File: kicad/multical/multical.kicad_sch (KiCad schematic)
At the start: 55 parts, among them J10 Screw_Terminal_01x02, J11 Screw_Terminal_01x02, J12 Screw_Terminal_01x02, J13 Screw_Terminal_01x02, J14 Screw_Terminal_01x02, J15 Screw_Terminal_01x02, J16 Screw_Terminal_01x02, J17 Screw_Terminal_01x02, J18 Screw_Terminal_01x02, K1 Relay_SPDT, K2 Relay_SPDT, K3 Relay_SPDT, K4 Relay_SPDT, K5 Relay_SPDT, K6 Relay_SPDT, K7 Relay_SPDT, K8 Relay_SPDT, U1 ESP32-WROOM-32, U10 HLK-PM01, U11 AMS1117-3.3, U12 zmpt101b, U13 ULN2003A, U14 ULN2003A, U2 ACS712xLCTR-20A, U3 ACS712xLCTR-20A, U4 ACS712xLCTR-20A, U5 ACS712xLCTR-20A, U6 ACS712xLCTR-20A, U7 ACS712xLCTR-20A, U8 ACS712xLCTR-20A, U9 ACS712xLCTR-20A

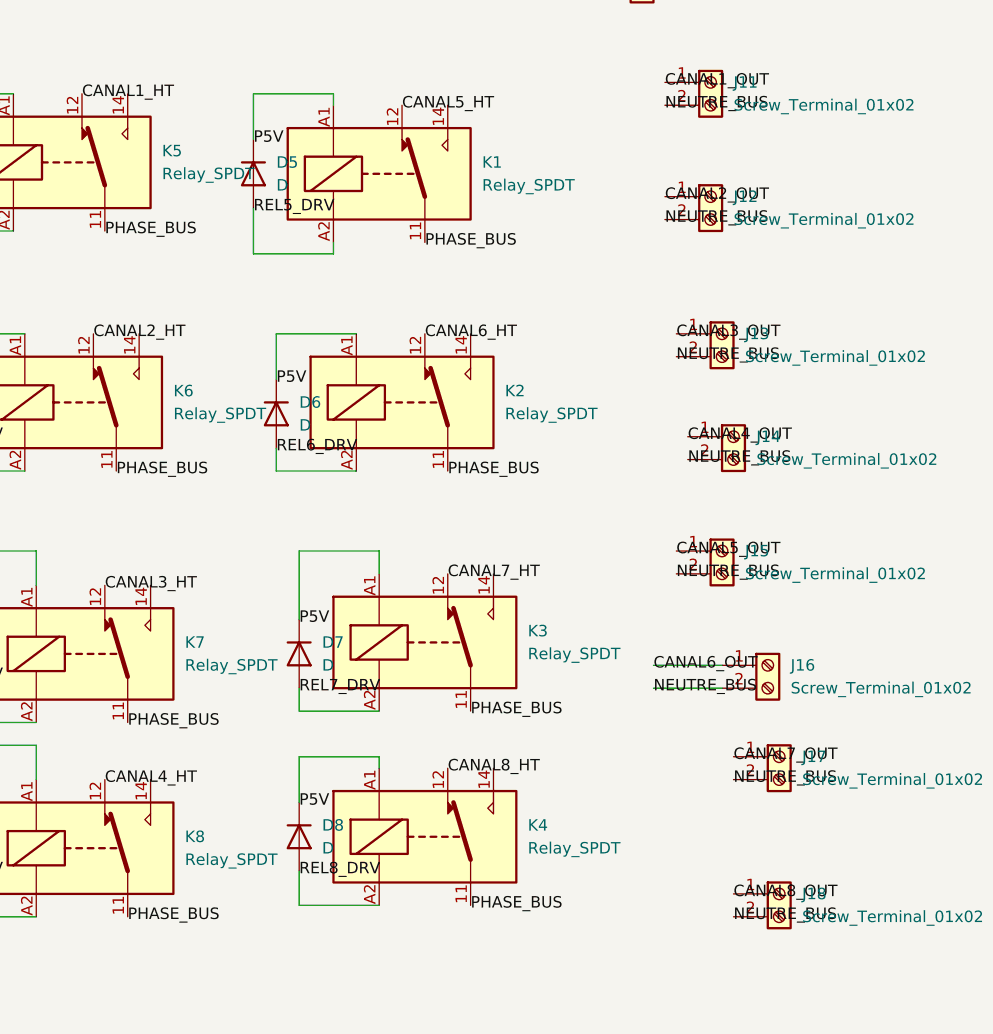
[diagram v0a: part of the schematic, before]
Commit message: Routage PCB 20A, schema de branchement et mise a jour de la presentation
- kicad/ : outils et guide de routage pour tenir 20A (GUIDE_ROUTAGE_20A,
  fix_dsn_widths_20A.py, replan_pcb_20A.py, strip_tracks.py), PCB/schema
  mis a jour en consequence. Routage non termine : il reste 10 pistes a
  tracer (cf. README racine).
- schema_branchement.png et diagramme_cas_utilisation.drawio ajoutes
- presentation de soutenance et GUIDE_MAQUETTE_BOITIER mis a jour
- retire l'ancienne sauvegarde du rapport (avant corrections)

Co-Authored-By: Claude Sonnet 5 <noreply@anthropic.com>
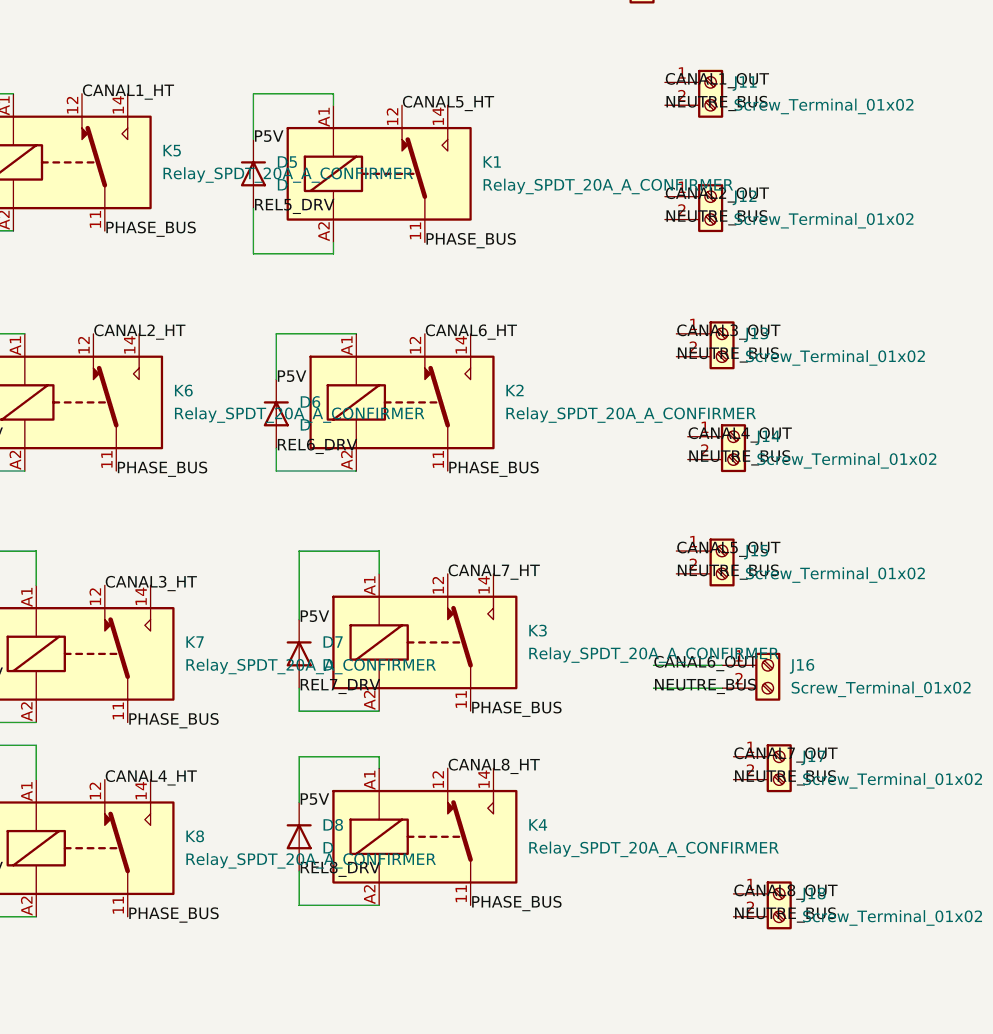
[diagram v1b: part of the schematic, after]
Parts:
- K1, K2, K3, K4, K5, K6, K7, K8: value Relay_SPDT -> Relay_SPDT_20A_A_CONFIRMER
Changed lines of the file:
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@@
 			)
 		)
-		(property "Value" "Relay_SPDT"
+		(property "Value" "Relay_SPDT_20A_A_CONFIRMER"
 			(at 210.82 119.3799 0)
 			(show_name no)
@@
 			)
 		)
-		(property "Value" "Relay_SPDT"
+		(property "Value" "Relay_SPDT_20A_A_CONFIRMER"
 			(at 243.84 44.4499 0)
 			(show_name no)
@@
 			)
 		)
-		(property "Value" "Relay_SPDT"
+		(property "Value" "Relay_SPDT_20A_A_CONFIRMER"
 			(at 246.38 69.8499 0)
 			(show_name no)
@@
 			)
 		)
-		(property "Value" "Relay_SPDT"
+		(property "Value" "Relay_SPDT_20A_A_CONFIRMER"
 			(at 209.55 69.8499 0)
 			(show_name no)
@@
 			)
 		)
-		(property "Value" "Relay_SPDT"
+		(property "Value" "Relay_SPDT_20A_A_CONFIRMER"
 			(at 248.92 118.1099 0)
 			(show_name no)
@@
 			)
 		)
-		(property "Value" "Relay_SPDT"
+		(property "Value" "Relay_SPDT_20A_A_CONFIRMER"
 			(at 248.92 96.5199 0)
 			(show_name no)
@@
 			)
 		)
-		(property "Value" "Relay_SPDT"
+		(property "Value" "Relay_SPDT_20A_A_CONFIRMER"
 			(at 208.28 43.1799 0)
 			(show_name no)
@@
 			)
 		)
-		(property "Value" "Relay_SPDT"
+		(property "Value" "Relay_SPDT_20A_A_CONFIRMER"
 			(at 210.82 97.7899 0)
 			(show_name no)
